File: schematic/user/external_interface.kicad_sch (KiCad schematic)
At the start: 27 parts, among them J2 Radio_Jack, J3 User_Jack, J5 PTT Breakout, Q3 MBT3904DW1T1, Q4 MBT3904DW1T1, Q5 MBT3904DW1T1, SW3 PTT_Button, SW4 Mode_Button, SW5 Vol_Up_Button, SW6 Vol_Down_Button

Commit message: v0.5 board: use taller buttons to hopefully avoid need to build buttons into enclosure.
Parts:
- SW3, SW4, SW5, SW6: footprint Button_Switch_SMD:SW_SPST_TL3342 -> Button_Switch_SMD:SW_SPST_TL3305C; LCSC C2886898 -> C2886904
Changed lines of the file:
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@@
     (property "Reference" "SW3" (id 0) (at 30.099 149.86 0))
     (property "Value" "PTT_Button" (id 1) (at 27.7876 149.86 0))
-    (property "Footprint" "Button_Switch_SMD:SW_SPST_TL3342" (id 2) (at 27.94 149.86 0)
-      (effects (font (size 1.27 1.27)) hide)
-    )
-    (property "Datasheet" "https://datasheet.lcsc.com/lcsc/2109061530_E-Switch-TL3342F160QG_C2886898.pdf" (id 3) (at 27.94 149.86 0)
-      (effects (font (size 1.27 1.27)) hide)
-    )
-    (property "LCSC" "C2886898" (id 4) (at 22.86 149.86 0)
+    (property "Footprint" "Button_Switch_SMD:SW_SPST_TL3305C" (id 2) (at 27.94 149.86 0)
+      (effects (font (size 1.27 1.27)) hide)
+    )
+    (property "Datasheet" "https://datasheet.lcsc.com/lcsc/2202251630_E-Switch-TL3305CF260QG_C2886904.pdf" (id 3) (at 27.94 149.86 0)
+      (effects (font (size 1.27 1.27)) hide)
+    )
+    (property "LCSC" "C2886904" (id 4) (at 22.86 149.86 0)
       (effects (font (size 1.27 1.27)) hide)
     )
@@
     (property "Reference" "SW5" (id 0) (at 73.279 149.86 0))
     (property "Value" "Vol_Up_Button" (id 1) (at 70.9676 149.86 0))
-    (property "Footprint" "Button_Switch_SMD:SW_SPST_TL3342" (id 2) (at 71.12 149.86 0)
-      (effects (font (size 1.27 1.27)) hide)
-    )
-    (property "Datasheet" "https://datasheet.lcsc.com/lcsc/2109061530_E-Switch-TL3342F160QG_C2886898.pdf" (id 3) (at 71.12 149.86 0)
-      (effects (font (size 1.27 1.27)) hide)
-    )
-    (property "LCSC" "C2886898" (id 4) (at 66.04 149.86 0)
+    (property "Footprint" "Button_Switch_SMD:SW_SPST_TL3305C" (id 2) (at 71.12 149.86 0)
+      (effects (font (size 1.27 1.27)) hide)
+    )
+    (property "Datasheet" "https://datasheet.lcsc.com/lcsc/2202251630_E-Switch-TL3305CF260QG_C2886904.pdf" (id 3) (at 71.12 149.86 0)
+      (effects (font (size 1.27 1.27)) hide)
+    )
+    (property "LCSC" "C2886904" (id 4) (at 66.04 149.86 0)
       (effects (font (size 1.27 1.27)) hide)
     )
@@
     (property "Reference" "SW6" (id 0) (at 94.869 149.86 0))
     (property "Value" "Vol_Down_Button" (id 1) (at 92.5576 149.86 0))
-    (property "Footprint" "Button_Switch_SMD:SW_SPST_TL3342" (id 2) (at 92.71 149.86 0)
-      (effects (font (size 1.27 1.27)) hide)
-    )
-    (property "Datasheet" "https://datasheet.lcsc.com/lcsc/2109061530_E-Switch-TL3342F160QG_C2886898.pdf" (id 3) (at 92.71 149.86 0)
-      (effects (font (size 1.27 1.27)) hide)
-    )
-    (property "LCSC" "C2886898" (id 4) (at 87.63 149.86 0)
+    (property "Footprint" "Button_Switch_SMD:SW_SPST_TL3305C" (id 2) (at 92.71 149.86 0)
+      (effects (font (size 1.27 1.27)) hide)
+    )
+    (property "Datasheet" "https://datasheet.lcsc.com/lcsc/2202251630_E-Switch-TL3305CF260QG_C2886904.pdf" (id 3) (at 92.71 149.86 0)
+      (effects (font (size 1.27 1.27)) hide)
+    )
+    (property "LCSC" "C2886904" (id 4) (at 87.63 149.86 0)
       (effects (font (size 1.27 1.27)) hide)
     )
@@
     (property "Reference" "SW4" (id 0) (at 50.419 149.86 0))
     (property "Value" "Mode_Button" (id 1) (at 48.1076 149.86 0))
-    (property "Footprint" "Button_Switch_SMD:SW_SPST_TL3342" (id 2) (at 48.26 149.86 0)
-      (effects (font (size 1.27 1.27)) hide)
-    )
-    (property "Datasheet" "https://datasheet.lcsc.com/lcsc/2109061530_E-Switch-TL3342F160QG_C2886898.pdf" (id 3) (at 48.26 149.86 0)
-      (effects (font (size 1.27 1.27)) hide)
-    )
-    (property "LCSC" "C2886898" (id 4) (at 43.18 149.86 0)
-      (effects (font (size 1.27 1.27)) hide)
-    )
+    (property "Footprint" "Button_Switch_SMD:SW_SPST_TL3305C" (id 2) (at 48.26 149.86 0)
+      (effects (font (size 1.27 1.27)) hide)
+    )
+    (property "Datasheet" "https://datasheet.lcsc.com/lcsc/2202251630_E-Switch-TL3305CF260QG_C2886904.pdf" (id 3) (at 48.26 149.86 0)
+      (effects (font (size 1.27 1.27)) hide)
+    )
+    (property "LCSC" "C2886904" (id 4) (at 43.18 149.86 0)
+      (effects (font (size 1.27 1.27)) hide)
+    )

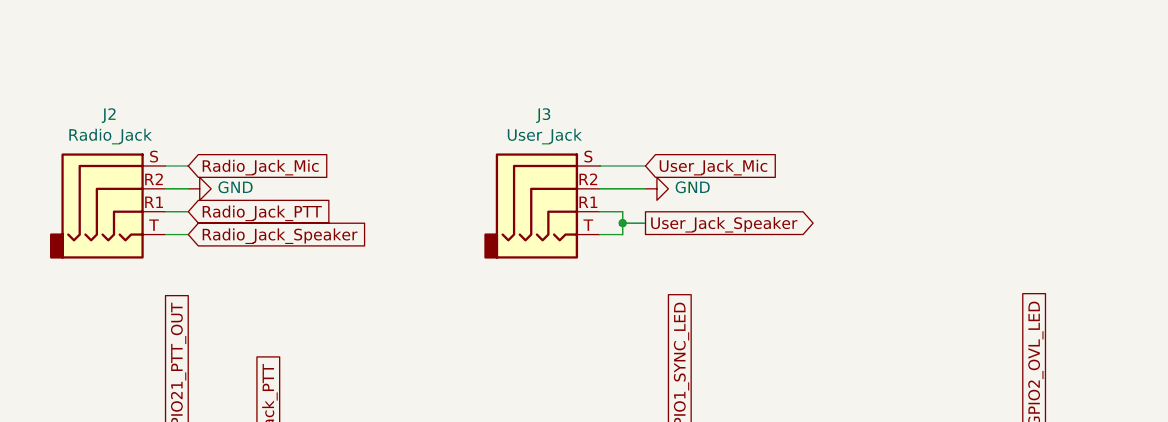
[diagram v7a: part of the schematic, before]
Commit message: v0.5 board: Switch to through hole part for radio/user jacks.
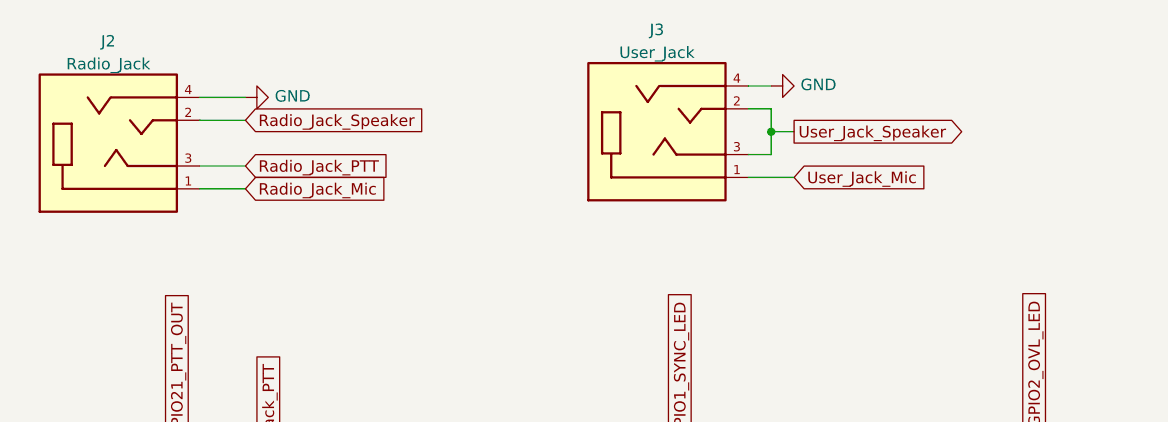
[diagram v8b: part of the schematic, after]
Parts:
- removed J2: Radio_Jack, Connector_Audio:Jack_3.5mm_PJ320D_Horizontal, symbol Connector:AudioJack4
- removed J3: User_Jack, Connector_Audio:Jack_3.5mm_PJ320D_Horizontal, symbol Connector:AudioJack4
- added J2: Radio_Jack, CUI_SJ-43514, symbol SJ-43514:SJ-43514
- added J3: User_Jack, CUI_SJ-43514, symbol SJ-43514:SJ-43514
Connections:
- net GND: now also J2.4, J3.4
- net Radio_Jack_Mic: now also J2.1
- net Radio_Jack_PTT: now also J2.3
- net Radio_Jack_Speaker: now also J2.2
- net User_Jack_Mic: now also J3.1
- net User_Jack_Speaker: now also J3.2, J3.3
